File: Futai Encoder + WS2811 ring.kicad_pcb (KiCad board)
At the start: 2 copper layers, 31 x 49 mm, 41 parts, among them J1 Conn_02x05_Top_Bottom, SW1 RotaryEncoder_Switch_RGB

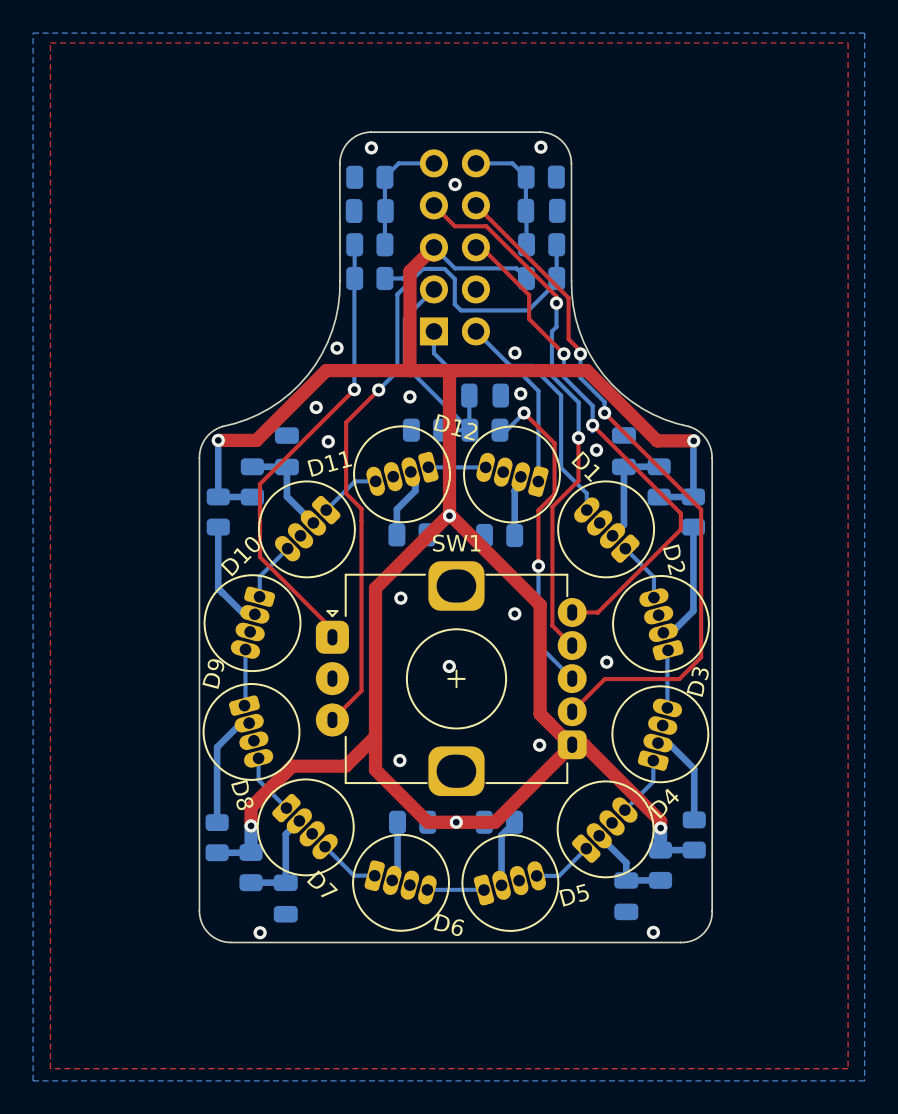
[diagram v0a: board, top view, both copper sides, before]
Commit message: v067: Resized silkscreens to 0.6, 100% aligned things to each other to satisfy my inner monk
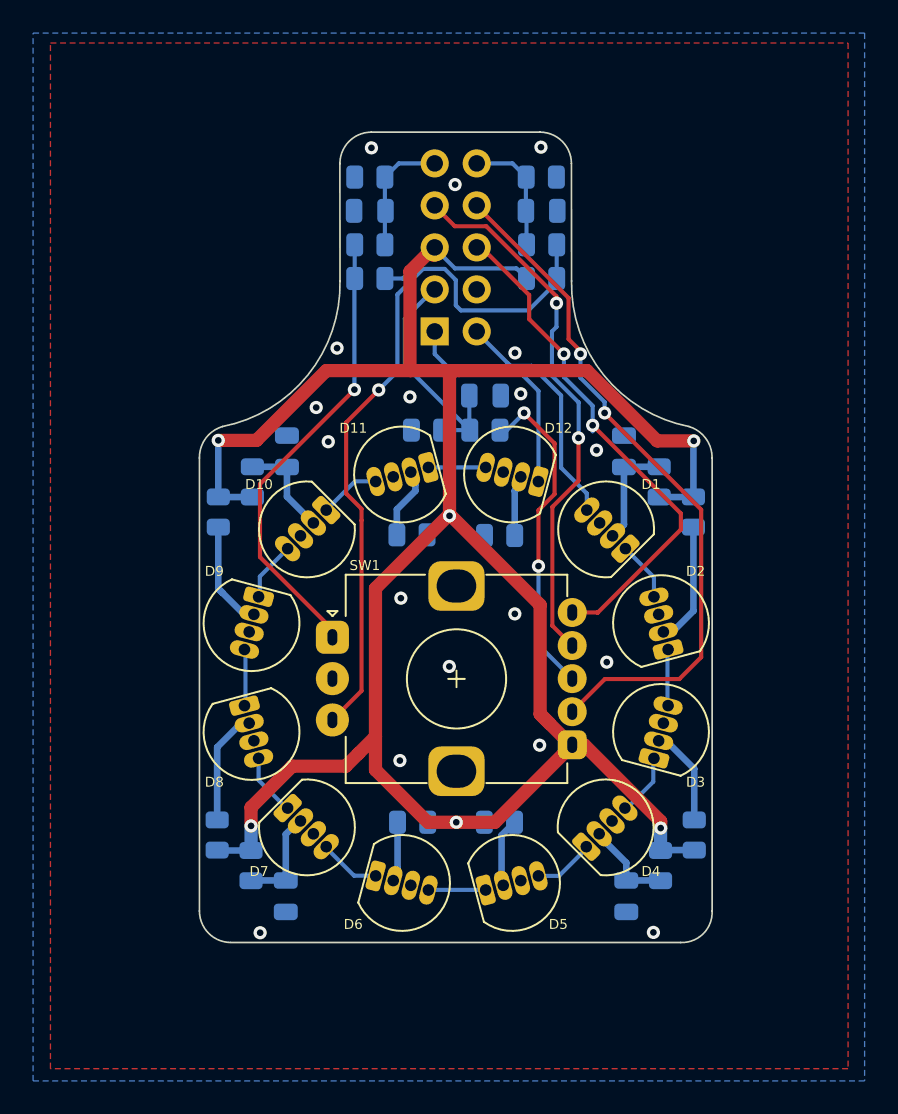
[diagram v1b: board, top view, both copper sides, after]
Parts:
- moved R8 0.16 mm to (134.1, 108.6)
- moved D3 0.15 mm to (160.9, 102.4)
- moved C7 0.14 mm to (138.2, 112.3)
- moved D4 0.12 mm to (157.6, 108.1)
- moved R7 0.12 mm to (136.1, 110.5)
- moved D5 0.10 mm to (151.9, 111.5)
- moved D7 0.07 mm to (139.5, 108.1)
- moved D6 0.06 mm to (145.2, 111.5)
- moved D9 0.06 mm to (136.2, 95.8)
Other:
- board text added: "+5V"
- board text added: "Blue"
- board text added: "DI"
- board text added: "DO"
- board text added: "Grn"
- board text added: "Red"
- board text added: "SW"
- board text added: "v0.67"
- board text removed: "5V"
- board text removed: "BLU"
- board text removed: "Din"
- board text removed: "Dout"
- board text removed: "GRE"
- board text removed: "RED"
- board text removed: "SWC"
- board text removed: "v0.65"
